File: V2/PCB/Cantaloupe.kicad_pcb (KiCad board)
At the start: 2 copper layers, 143.9 x 118.7 mm, 121 parts, among them J1 USB_In, J2 OLED, J3 Link, J4 Debug, J5 Trackball, Q1 2N7002, Q2 AO3401A, SW1 MX, SW10 MX, SW11 MX, SW12 MX, SW13 MX, SW14 MX, SW15 MX, SW16 MX, SW17 MX, SW18 MX, SW19 MX, SW2 MX, SW20 MX, SW21 MX, SW22 MX, SW23 MX, SW24 MX, SW25 MX, SW26 MX, SW27 MX, SW28 MX, SW29 MX, SW3 MX, SW30 MX, SW31 Encoder, SW32 MX, SW4 MX, SW5 MX, SW6 MX, SW7 MX, SW8 MX, SW9 MX, U1 STM32F4x1CxUx, U2 SRV0504, U3 SRV0504, U4 XC6206P332MR, U5 LMV321, Y1 8MHz

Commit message: Tentative V2.1 update
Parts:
- added R19: 4.7k, Resistor_SMD:R_0603_1608Metric, B.Cu at (144.8, 74.4)
- added R20: 4.7k, Resistor_SMD:R_0603_1608Metric, B.Cu at (141.3, 74.4)
- A1: footprint Ariamelon:Catmelon -> Ariamelon:Ariamelon_Logo_x2
- J5: value Trackball -> Trackpad; footprint Ariamelon:pimoroni_trackball_flippable -> Ariamelon:FPC-SMD_FPC05012-09200-.5mm-rev
- moved J5 11.8 mm to (154.8, 88.5)
- moved A1 5.58 mm to (143.0, 57.5)
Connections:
- J5 pad 2: SDA -> GND
- J5 pad 3: SCL -> SDA
- J5 pad 5: GND -> unconnected-(J5-Pad5)
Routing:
- net SDA: track 39.6 -> 63.7 mm
- net VDD: track 162.4 -> 182.4 mm, vias 10 -> 13
- net SCL: track 38.9 -> 58.8 mm, vias 2 -> 4
- net GND: track 30.0 -> 13.2 mm, vias 88 -> 93
- net Side: track 11.7 -> 9.40 mm
- net Net-(D24-Pad2): track 2.81 -> 1.55 mm
- net Net-(D20-Pad2): track 2.81 -> 1.55 mm
- net Net-(D12-Pad2): track 2.81 -> 1.55 mm
- net Net-(D3-Pad2): track 2.81 -> 1.55 mm
- net Net-(D21-Pad2): track 2.81 -> 1.55 mm
- net Net-(D2-Pad2): track 2.81 -> 1.55 mm
- net Net-(D18-Pad2): track 2.81 -> 1.55 mm
- net Net-(D13-Pad2): track 2.81 -> 1.55 mm
- net Net-(D1-Pad2): track 2.81 -> 1.55 mm
- net Net-(D6-Pad2): track 2.81 -> 1.55 mm
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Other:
- outline, holes or cut-outs redrawn
- board text added: "Cantaloupe V2.1"
- board text added: "Trackpad"
- board text removed: "Cantaloupe V2.0 Aria"
- board text removed: "Trackball"

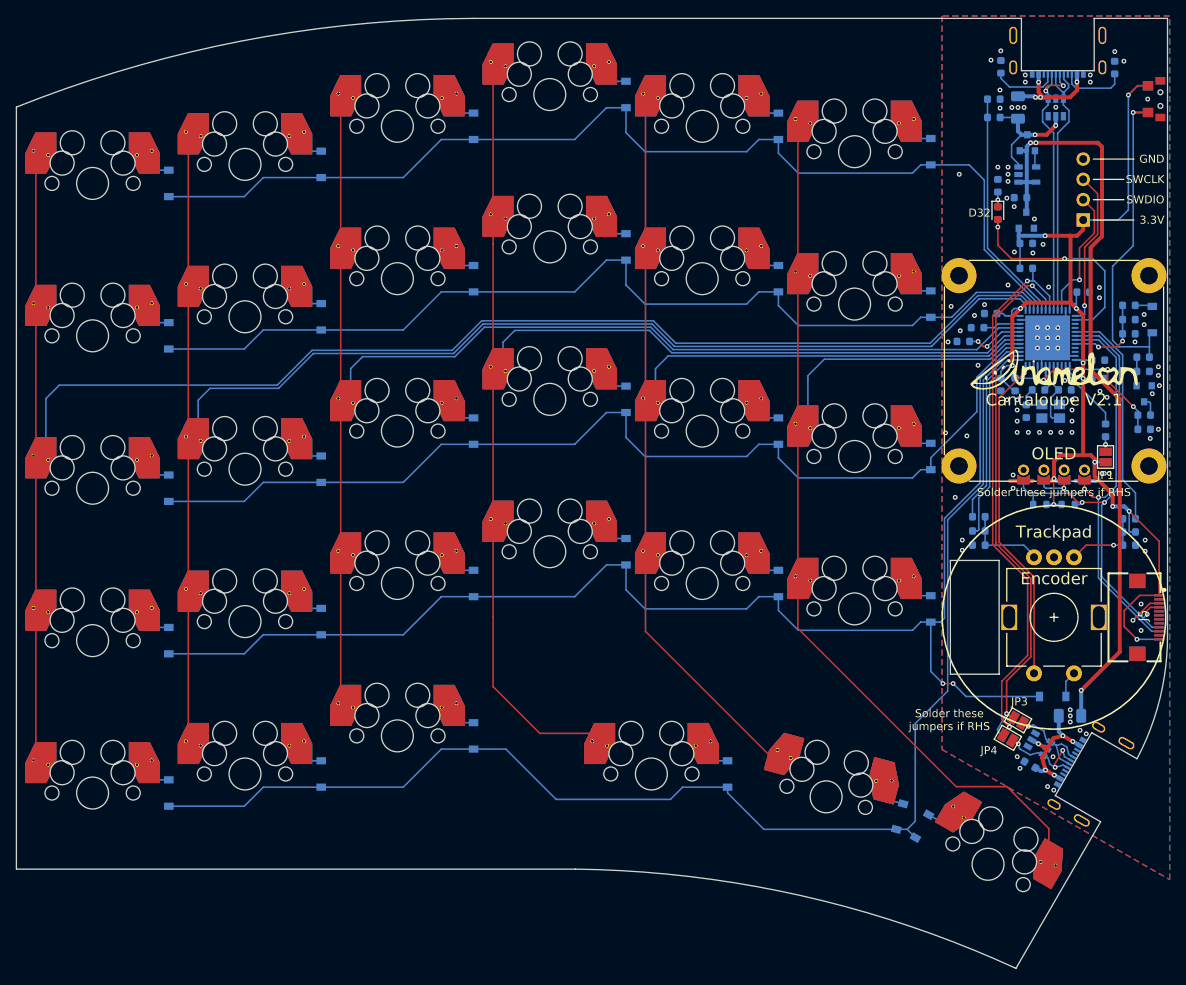
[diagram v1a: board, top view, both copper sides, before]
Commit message: Revert "Tentative V2.1 update"
This reverts commit 42b4223a0f1e602d13e2d92696f419f95c71691f.
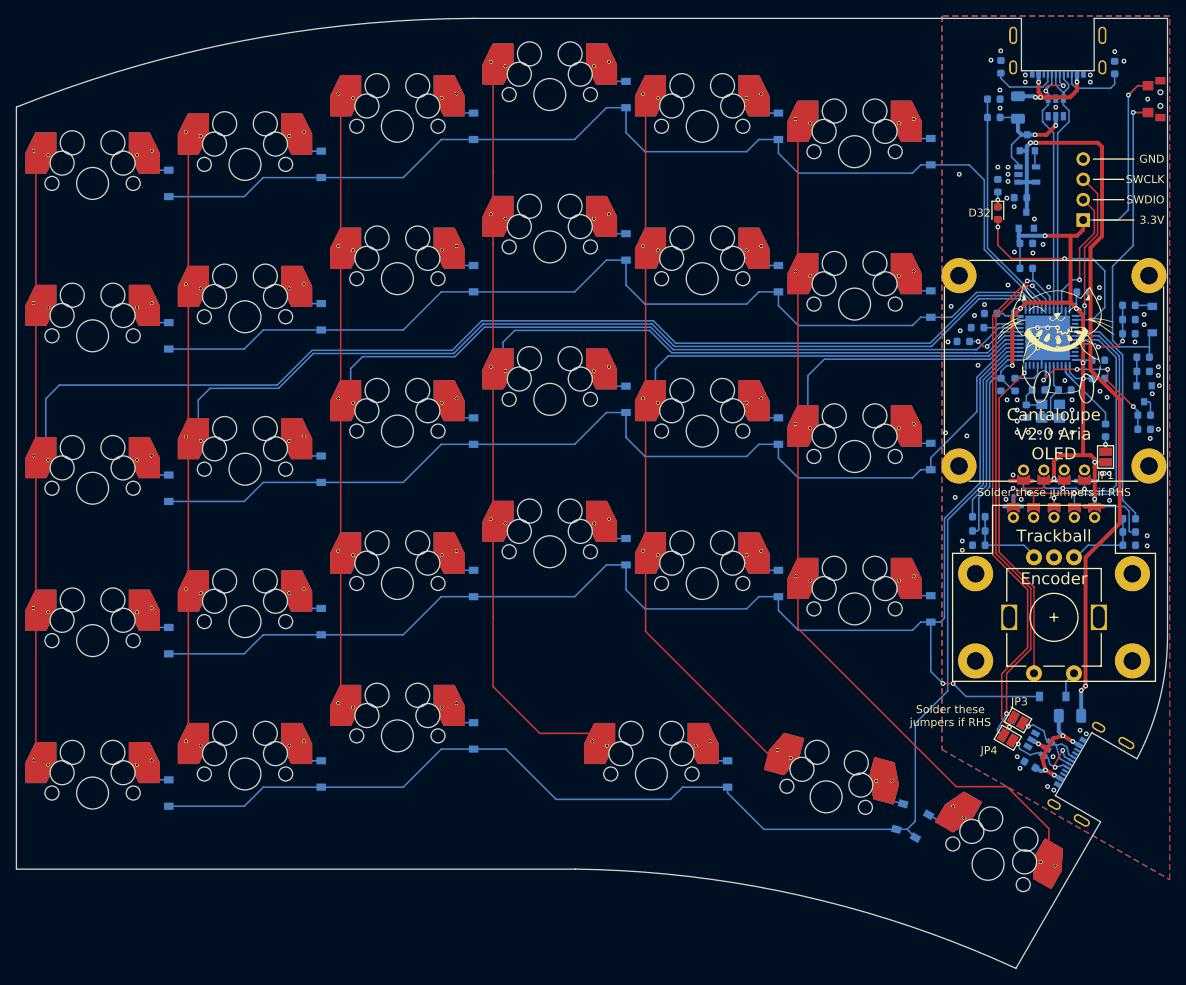
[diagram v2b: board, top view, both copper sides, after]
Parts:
- removed R19, R20: 4.7k, Resistor_SMD:R_0603_1608Metric
- A1: footprint Ariamelon:Ariamelon_Logo_x2 -> Ariamelon:Catmelon
- J5: value Trackpad -> Trackball; footprint Ariamelon:FPC-SMD_FPC05012-09200-.5mm-rev -> Ariamelon:pimoroni_trackball_flippable
- moved J5 11.8 mm to (143.0, 88.5)
- moved A1 5.58 mm to (144.3, 52.1)
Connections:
- J5 pad 2: GND -> SDA
- J5 pad 3: SDA -> SCL
- J5 pad 5: unconnected-(J5-Pad5) -> GND
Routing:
- net SDA: track 63.7 -> 39.6 mm
- net VDD: track 182.4 -> 162.4 mm, vias 13 -> 10
- net SCL: track 58.8 -> 38.9 mm, vias 4 -> 2
- net GND: track 13.2 -> 30.0 mm, vias 93 -> 88
- net Side: track 9.40 -> 11.7 mm
- net Net-(D24-Pad2): track 1.55 -> 2.81 mm
- net Net-(D20-Pad2): track 1.55 -> 2.81 mm
- net Net-(D12-Pad2): track 1.55 -> 2.81 mm
- net Net-(D3-Pad2): track 1.55 -> 2.81 mm
- net Net-(D21-Pad2): track 1.55 -> 2.81 mm
- net Net-(D2-Pad2): track 1.55 -> 2.81 mm
- net Net-(D18-Pad2): track 1.55 -> 2.81 mm
- net Net-(D13-Pad2): track 1.55 -> 2.81 mm
- net Net-(D1-Pad2): track 1.55 -> 2.81 mm
- net Net-(D6-Pad2): track 1.55 -> 2.81 mm
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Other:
- outline, holes or cut-outs redrawn
- board text added: "Cantaloupe V2.0 Aria"
- board text added: "Trackball"
- board text removed: "Cantaloupe V2.1"
- board text removed: "Trackpad"
